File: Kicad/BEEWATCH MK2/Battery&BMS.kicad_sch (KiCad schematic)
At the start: 24 parts, among them Q3 DMP1045U-7, Q9 DMG6968U, U4 MCP73832-2-OT, U5 ME6217C33M5G, U8 S-1206B18-M3T1G

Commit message: Deep optmization 80% completed
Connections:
- net +VBAT: no longer R44.1
- net +VBAT_IN: now also R44.1
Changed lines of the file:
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@@
+		)
+	)
+	(label "+VBAT_IN"
+		(at 88.9 138.43 90)
+		(effects
+			(font
+				(size 1.27 1.27)
+			)
+			(justify left bottom)
 		)
 	)
@@
 					(unit 1)
 				)
-			)
-		)
-	)
-	(symbol
-		(lib_id "power:+5V")
-		(at 88.9 138.43 0)
-		(unit 1)
-		(exclude_from_sim no)
-		(in_bom yes)
-		(on_board yes)
-		(dnp no)
-		(fields_autoplaced yes)
-		(property "Reference" "#PWR029"
-			(at 88.9 142.24 0)
-			(effects
-				(font
-					(size 1.27 1.27)
-				)
-				(hide yes)
-			)
-		)
-		(property "Value" "+VBAT"
-			(at 88.9 134.62 0)
-			(effects
-				(font
-					(size 1.27 1.27)
-				)
-			)
-		)
-		(property "Footprint" ""
-			(at 88.9 138.43 0)
-			(effects
-				(font
-					(size 1.27 1.27)
-				)
-				(hide yes)
-			)
-		)
-		(property "Datasheet" ""
-			(at 88.9 138.43 0)
-			(effects
-				(font
-					(size 1.27 1.27)
-				)
-				(hide yes)
-			)
-		)
-		(property "Description" "Power symbol creates a global label with name \"+5V\""
-			(at 88.9 138.43 0)
-			(effects
-				(font
-					(size 1.27 1.27)
-				)
-				(hide yes)
-			)
-		)
-		(pin "1"
-		)
-		(instances
-			(project "BEEWATCH MK3"
-				(path "/e9c5fb53-480b-4989-8495-a3341ee99514/d9595010-f994-473f-a0a5-39e7f06951fe"
-					(reference "#PWR029")
-					(unit 1)
-				)

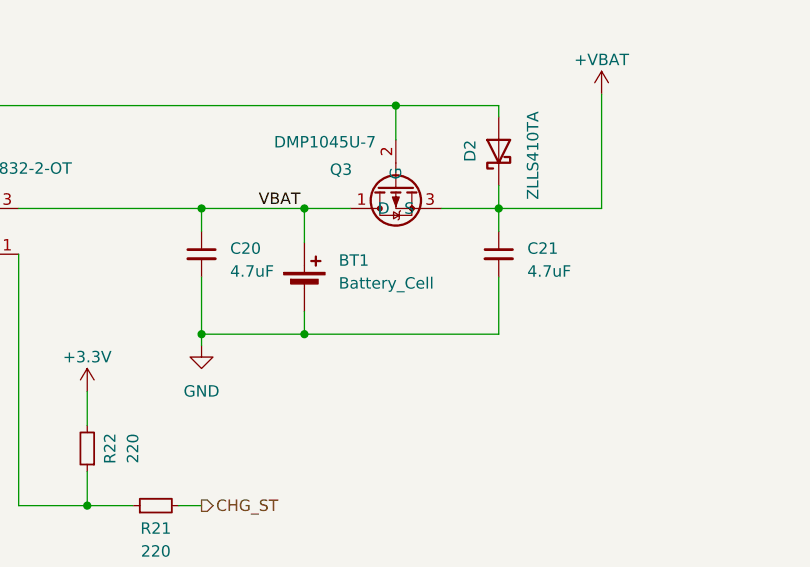
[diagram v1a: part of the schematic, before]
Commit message: Antenna and Schematic correction
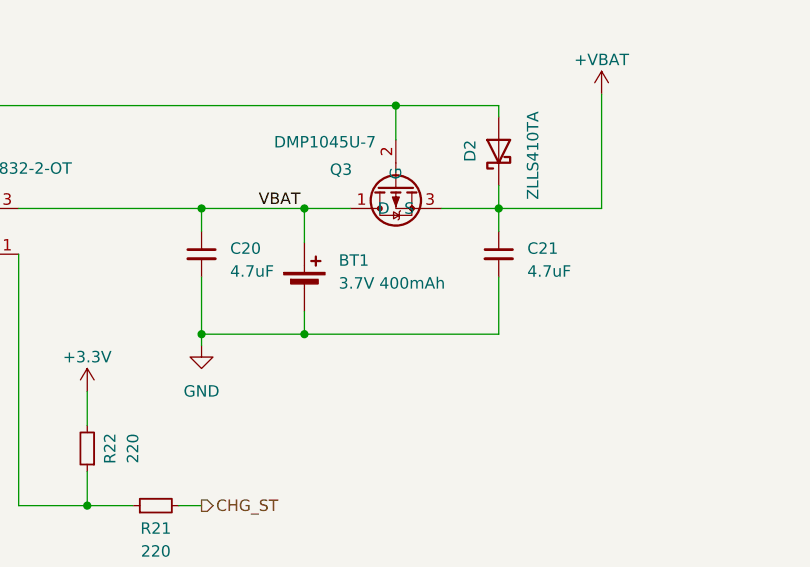
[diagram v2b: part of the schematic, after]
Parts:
- BT1: value Battery_Cell -> 3.7V 400mAh
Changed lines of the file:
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@@
 			)
 		)
-		(property "Value" "Battery_Cell"
+		(property "Value" "3.7V 400mAh"
 			(at 111.76 69.2784 0)
 			(effects

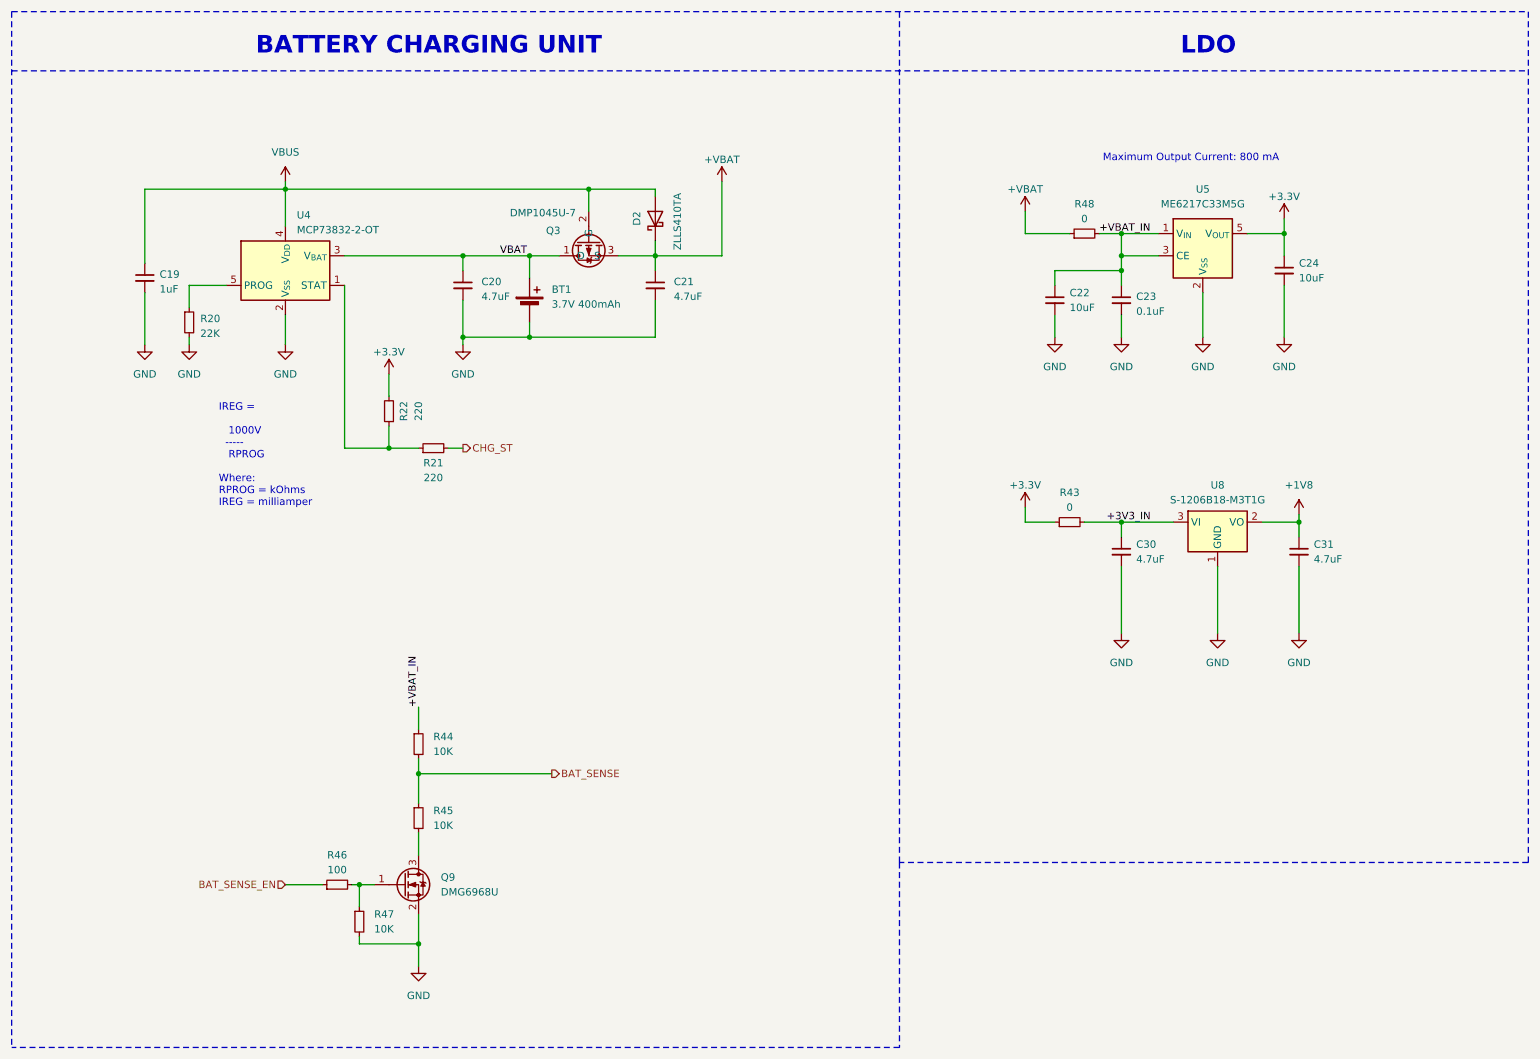
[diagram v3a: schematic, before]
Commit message: Updating MPN
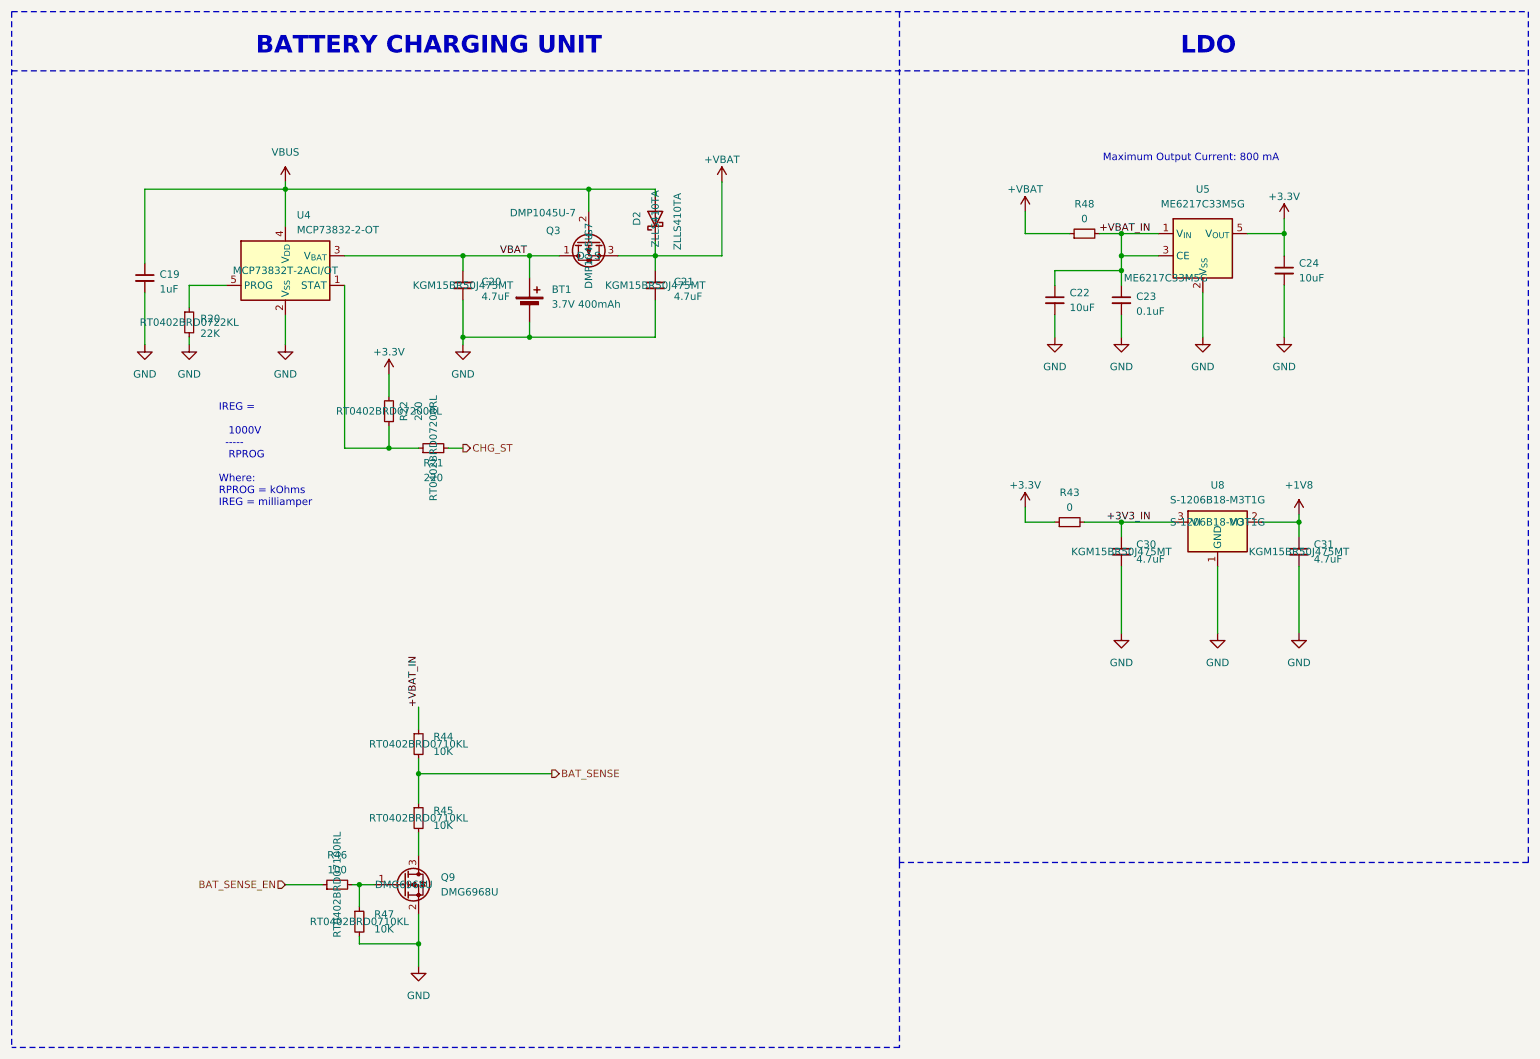
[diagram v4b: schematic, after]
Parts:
- C20, C21, C30, C31: MPN (none) -> KGM15BR50J475MT
- D2: MPN (none) -> ZLLS410TA
- Q3: MPN (none) -> DMP1045U-7
- Q9: MPN (none) -> DMG6968U
- R20: MPN (none) -> RT0402BRD0722KL
- R21, R22: MPN (none) -> RT0402BRD07200RL
- R44, R45, R47: MPN (none) -> RT0402BRD0710KL
- R46: MPN (none) -> RT0402BRD07100RL
- U4: MPN (none) -> MCP73832T-2ACI/OT
- U5: MPN (none) -> ME6217C33M5G
- U8: MPN (none) -> S-1206B18-M3T1G
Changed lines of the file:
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@@
 			)
 		)
-		(property "MPN" ""
+		(property "MPN" "DMP1045U-7"
 			(at 118.11 60.96 0)
 			(effects
@@
 			)
 		)
-		(property "MPN" ""
+		(property "MPN" "ME6217C33M5G"
 			(at 217.17 64.77 0)
 			(effects
@@
 			)
 		)
-		(property "MPN" ""
+		(property "MPN" "RT0402BRD0710KL "
 			(at 78.74 175.26 0)
 			(effects
@@
 			)
 		)
-		(property "MPN" ""
+		(property "MPN" "ZLLS410TA"
 			(at 129.54 54.61 0)
 			(effects
@@
 			)
 		)
-		(property "MPN" ""
+		(property "MPN" "RT0402BRD07200RL "
 			(at 83.82 87.63 0)
 			(effects
@@
 			)
 		)
-		(property "MPN" ""
+		(property "MPN" "RT0402BRD0710KL "
 			(at 88.9 144.78 0)
 			(effects
@@
 			)
 		)
-		(property "MPN" ""
+		(property "MPN" "KGM15BR50J475MT "
 			(at 96.52 66.04 0)
 			(effects
@@
 			)
 		)
-		(property "MPN" ""
+		(property "MPN" "RT0402BRD07100RL "
 			(at 74.93 168.91 0)
 			(effects
@@
 			)
 		)
-		(property "MPN" ""
+		(property "MPN" "RT0402BRD0710KL "
 			(at 88.9 157.48 0)
 			(effects
@@
 			)
 		)
-		(property "MPN" ""
+		(property "MPN" "RT0402BRD0722KL "
 			(at 49.53 72.39 0)
 			(effects
@@
 			)
 		)
-		(property "MPN" ""
+		(property "MPN" "RT0402BRD07200RL "
 			(at 91.44 93.98 0)
 			(effects
@@
 			)
 		)
-		(property "MPN" ""
+		(property "MPN" "DMG6968U"
 			(at 86.36 168.91 0)
 			(effects
@@
 			)
 		)
-		(property "MPN" ""
+		(property "MPN" "MCP73832T-2ACI/OT"
 			(at 66.04 63.5 0)
 			(effects
@@
 			)
 		)
-		(property "MPN" ""
+		(property "MPN" "KGM15BR50J475MT "
 			(at 129.54 66.04 0)
 			(effects
@@
 			)
 		)
-		(property "MPN" ""
+		(property "MPN" "S-1206B18-M3T1G"
 			(at 226.06 106.68 0)
 			(effects
@@
 			)
 		)
-		(property "MPN" ""
+		(property "MPN" "KGM15BR50J475MT "
 			(at 240.03 111.76 0)
 			(effects
@@
 			)
 		)
-		(property "MPN" ""
+		(property "MPN" "KGM15BR50J475MT "
 			(at 209.55 111.76 0)
 			(effects
